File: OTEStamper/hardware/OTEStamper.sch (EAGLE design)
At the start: 67 parts, among them Q1 MMBT3904LT1G, Q2 MMBT3904LT1G, Q3 Si4825DDY, Q4 DMG2305UX, Q5 DMMT5401, U1 AP62500SJ-7, U2 SN74AUP1T57DBVR, U3 ATMEGA328PB_AU(32TQFP), U4 SN74LVC1G123DCTR, X1 PJ-063AH, X2 ADAFRUIT_2222, X3 522710479

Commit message: OTEStamper Board Revision 1.0.0
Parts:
- added C15: 150uF 25V UCM1E151MCL1GS, rcl:CPOL-EUUD-6,3X7,7
- JP2, JP3: value DNP -> PRPC002SBBN-M71RC
- Q1, Q2: value MMBT3904LT1G -> MMBT2222A-TP
- X3: value 522710479 -> S2B-PH-SM4-TB(LF)(SN); device SkyFall:522710479 -> SkyFall:S2B-PH-SM4-TB(LF)(SN)
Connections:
- net +12V: now also X3.1
- net 0V: now also C15.-; no longer X3.4
- net 12V_MONITOR: now also C15.+
- net LED: no longer X3.1
- net XVS: no longer X3.3
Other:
- note added: "Author: Mark Simpson @ChasinSpin Confidential Version: 1.0.0"
- note added: "Fan Max Current: 500mA"
- note added: "If using LED signal, an appropriate inline resistor is required."
- note added: "Use 2 pin header on XVS and 0V and clip the 0V (but leave plastic retainer)"
- note removed: "4 POS FPC Molex Cable 151670711"
- note removed: "Author: Mark Simpson @ChasinSpin Confidential Version: 0.9b"
- note removed: "DNP - For manual wiring if needed"
- note removed: "Fan Max Current: 150mA"
- note removed: "LED resistor is on camera board"
- moved on the sheet: C1, F1, Q3, X1

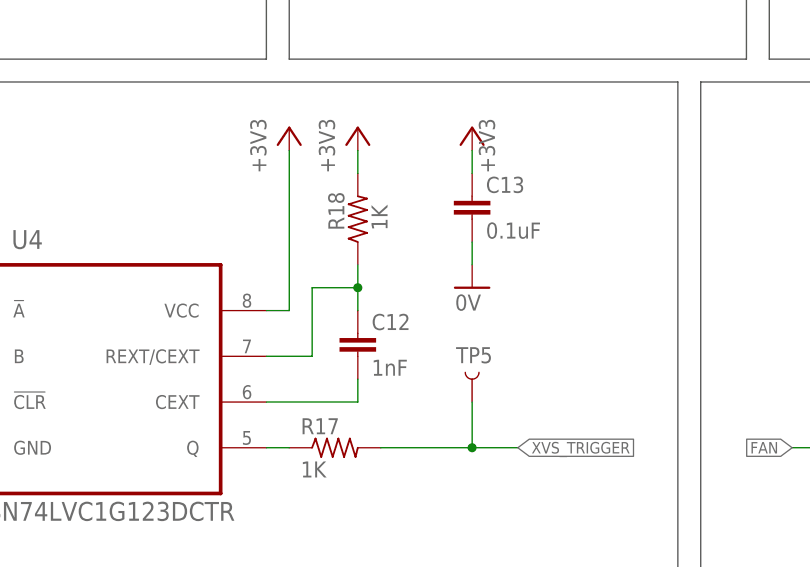
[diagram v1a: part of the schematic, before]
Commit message: Extending XVS monostable pulse extender from 1.2uS to 1ms, to account for different camera boards with different XVS pulse lengths.
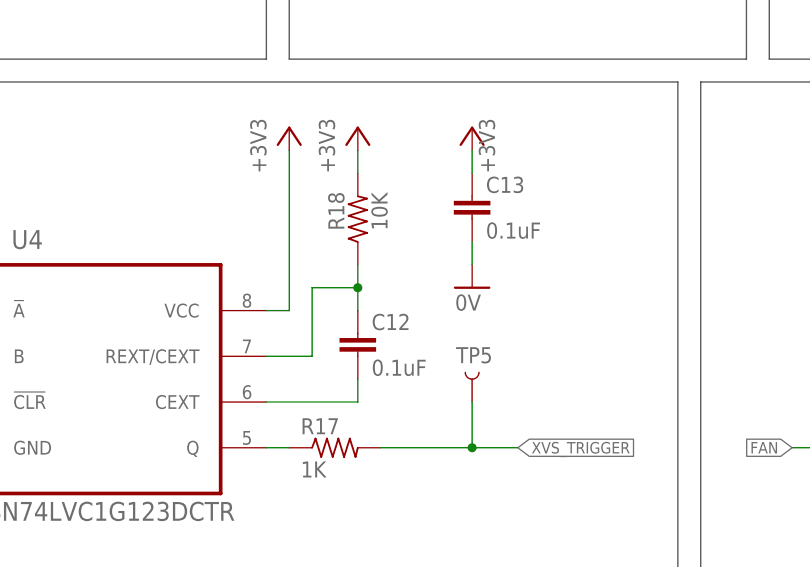
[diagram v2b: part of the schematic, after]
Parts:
- C12: value 1nF -> 0.1uF
- R18: value 1K -> 10K
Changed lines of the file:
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@@
 <part name="GND16" library="SkyFall" library_urn="urn:adsk.eagle:library:9574203" deviceset="0V" device=""/>
 <part name="+3V12" library="SkyFall" library_urn="urn:adsk.eagle:library:9574203" deviceset="+3V3" device=""/>
-<part name="C12" library="SkyFall" library_urn="urn:adsk.eagle:library:9574203" deviceset="C-EU" device="" package3d_urn="urn:adsk.eagle:package:23680/2" value="1nF"/>
-<part name="R18" library="SkyFall" library_urn="urn:adsk.eagle:library:9574203" deviceset="R-US" device="" package3d_urn="urn:adsk.eagle:package:6297178/3" value="1K"/>
+<part name="C12" library="SkyFall" library_urn="urn:adsk.eagle:library:9574203" deviceset="C-EU" device="" package3d_urn="urn:adsk.eagle:package:23680/2" value="0.1uF"/>
+<part name="R18" library="SkyFall" library_urn="urn:adsk.eagle:library:9574203" deviceset="R-US" device="" package3d_urn="urn:adsk.eagle:package:6297178/3" value="10K"/>
 <part name="+3V13" library="SkyFall" library_urn="urn:adsk.eagle:library:9574203" deviceset="+3V3" device=""/>
 <part name="U3" library="SkyFall" library_urn="urn:adsk.eagle:library:9574203" deviceset="ATMEGA328PB_TQFP" device="" package3d_urn="urn:adsk.eagle:package:40732480/2" value="ATMEGA328PB_AU(32TQFP)"/>
